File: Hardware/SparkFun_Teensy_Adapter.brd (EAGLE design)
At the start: 53.3 x 59.7 mm, 19 parts, among them U1 5V

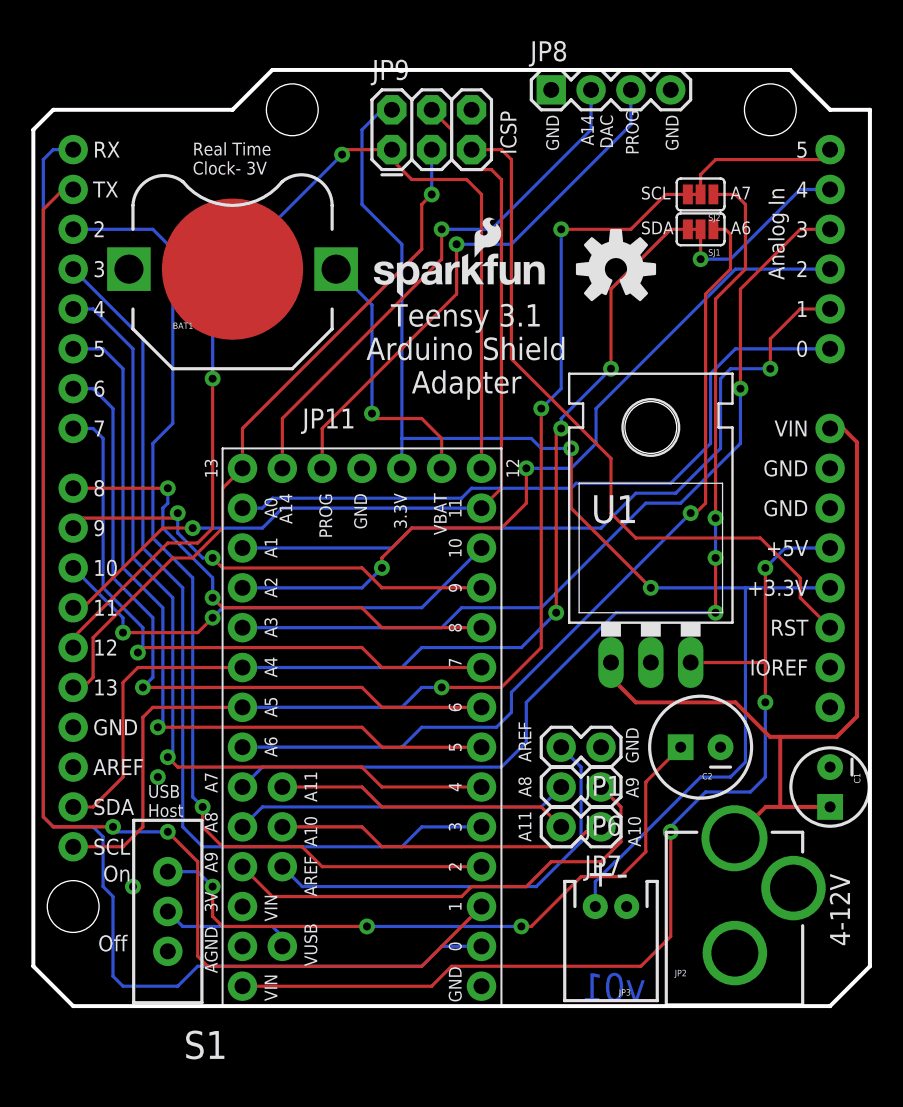
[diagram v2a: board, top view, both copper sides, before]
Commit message: Moving vias from under regulator, removing USB host shield parts
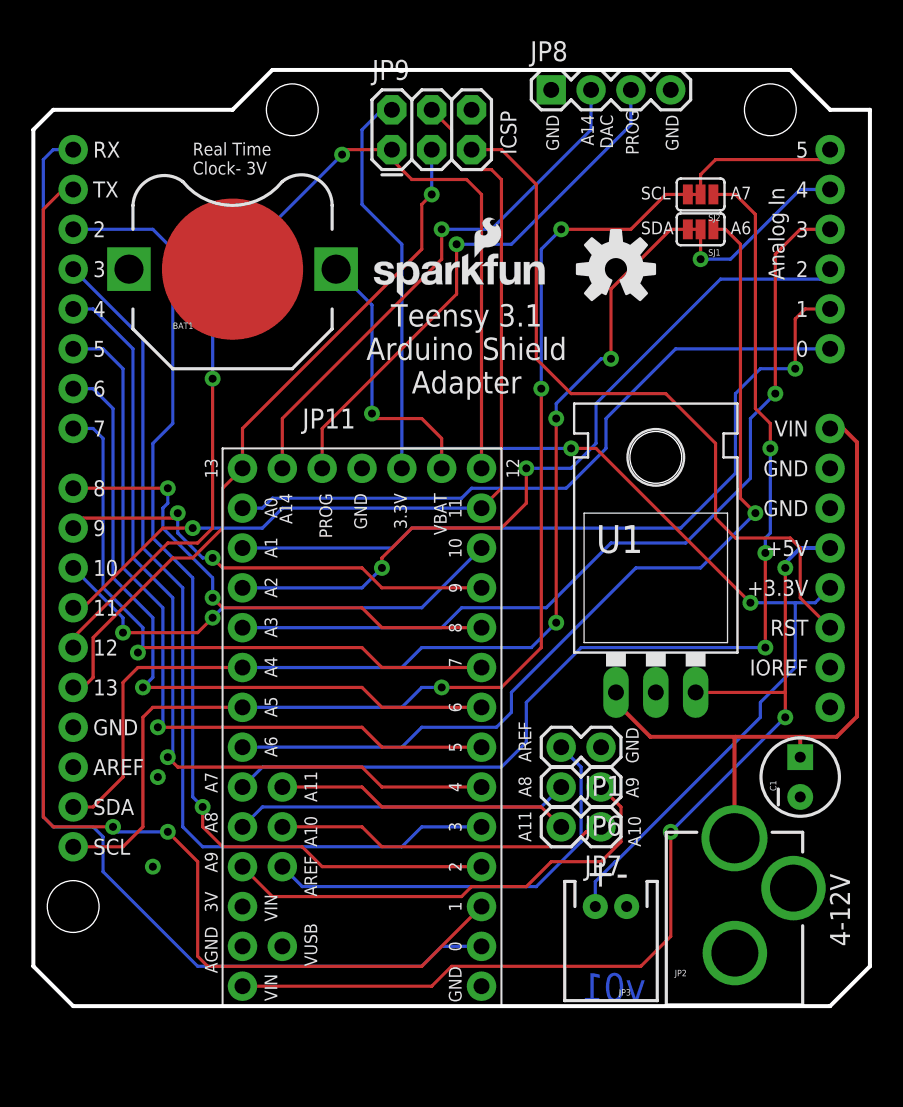
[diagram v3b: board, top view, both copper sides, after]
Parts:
- removed C2: 100uF, SparkFun-Capacitors:CPOL-RADIAL-100UF-25V
- removed S1: (no value), SparkFun-Electromechanical:SWITCH-SPDT
- JP1, JP6, JP7: value M02PTH -> (none)
- JP11: value TEENSY-3.1 -> TEENSY-3.1SILK
- JP3: value M02JST-PTH-2 -> (none)
- moved C1 2.01 mm to (51.4, 31.1), turned to 90 degrees
- moved U1 1.93 mm to (42.2, 40.3)
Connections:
- removed net N$1: C2.1, S1.3
- net GND: no longer C2.2
- net VUSB: no longer S1.2
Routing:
- net N$1: track 42.6 -> 0.00 mm, vias 3 -> 0
- net VUSB: track 8.60 -> 0.00 mm
- net VRAW: track 49.7 -> 44.8 mm
- net RX: track 82.4 -> 77.8 mm
- net A7: track 65.4 -> 69.9 mm
- net A6: track 55.7 -> 59.3 mm
- net 3.3V: track 84.0 -> 81.5 mm
- net A3: track 53.8 -> 55.4 mm
- net A0: track 44.3 -> 42.8 mm
- net 5V: track 65.7 -> 64.4 mm
- net A1: track 47.5 -> 48.6 mm
- net RESET: track 45.7 -> 46.6 mm
- net SDA: track 68.0 -> 68.8 mm
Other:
- board text removed: "Off"
- board text removed: "On"
- board text removed: "USB Host"

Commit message: Updates for QC final review before reds
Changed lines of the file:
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@@
 <setting verticaltext="up"/>
 </settings>
-<grid distance="0.0125" unitdist="inch" unit="inch" style="lines" multiple="1" display="yes" altdistance="0.005" altunitdist="inch" altunit="inch"/>
+<grid distance="0.05" unitdist="inch" unit="inch" style="lines" multiple="1" display="yes" altdistance="0.005" altunitdist="inch" altunit="inch"/>
 <layers>
 <layer number="1" name="Top" color="4" fill="1" visible="yes" active="yes"/>
@@
 <layer number="47" name="Measures" color="7" fill="1" visible="no" active="yes"/>
 <layer number="48" name="Document" color="7" fill="1" visible="no" active="yes"/>
-<layer number="49" name="Reference" color="7" fill="1" visible="no" active="yes"/>
+<layer number="49" name="Reference" color="7" fill="1" visible="yes" active="yes"/>
 <layer number="50" name="dxf" color="7" fill="1" visible="no" active="no"/>
 <layer number="51" name="tDocu" color="6" fill="1" visible="yes" active="yes"/>
@@
 <layer number="127" name="_tValues" color="7" fill="1" visible="no" active="yes"/>
 <layer number="128" name="_bValues" color="7" fill="1" visible="no" active="yes"/>
-<layer number="129" name="Mask" color="7" fill="1" visible="yes" active="yes"/>
+<layer number="129" name="Mask" color="7" fill="1" visible="no" active="yes"/>
 <layer number="131" name="tAdjust" color="7" fill="1" visible="no" active="yes"/>
 <layer number="132" name="bAdjust" color="7" fill="1" visible="no" active="yes"/>
@@
 Clock- 3V</text>
 <text x="33.3375" y="70.8025" size="1.016" layer="21" font="vector" ratio="15" rot="R90">ICSP</text>
-<wire x1="2.54" y1="19.05" x2="5.08" y2="16.51" width="0.254" layer="20"/>
-<wire x1="5.08" y1="16.51" x2="53.34" y2="16.51" width="0.254" layer="20"/>
-<wire x1="53.34" y1="16.51" x2="55.88" y2="19.05" width="0.254" layer="20"/>
-<wire x1="55.88" y1="19.05" x2="55.88" y2="73.66" width="0.254" layer="20"/>
-<wire x1="55.88" y1="73.66" x2="53.34" y2="73.66" width="0.254" layer="20"/>
-<wire x1="53.34" y1="73.66" x2="50.8" y2="76.2" width="0.254" layer="20"/>
-<wire x1="50.8" y1="76.2" x2="17.78" y2="76.2" width="0.254" layer="20"/>
-<wire x1="17.78" y1="76.2" x2="15.24" y2="73.66" width="0.254" layer="20"/>
-<wire x1="15.24" y1="73.66" x2="3.81" y2="73.66" width="0.254" layer="20"/>
-<wire x1="3.81" y1="73.66" x2="2.54" y2="72.39" width="0.254" layer="20"/>
-<wire x1="2.54" y1="72.39" x2="2.54" y2="19.05" width="0.254" layer="20"/>
+<wire x1="2.54" y1="19.05" x2="5.08" y2="16.51" width="0.2032" layer="20"/>
+<wire x1="5.08" y1="16.51" x2="53.34" y2="16.51" width="0.2032" layer="20"/>
+<wire x1="53.34" y1="16.51" x2="55.88" y2="19.05" width="0.2032" layer="20"/>
+<wire x1="55.88" y1="19.05" x2="55.88" y2="73.66" width="0.2032" layer="20"/>
+<wire x1="55.88" y1="73.66" x2="53.34" y2="73.66" width="0.2032" layer="20"/>
+<wire x1="53.34" y1="73.66" x2="50.8" y2="76.2" width="0.2032" layer="20"/>
+<wire x1="50.8" y1="76.2" x2="17.78" y2="76.2" width="0.2032" layer="20"/>
+<wire x1="17.78" y1="76.2" x2="15.24" y2="73.66" width="0.2032" layer="20"/>
+<wire x1="15.24" y1="73.66" x2="3.81" y2="73.66" width="0.2032" layer="20"/>
+<wire x1="3.81" y1="73.66" x2="2.54" y2="72.39" width="0.2032" layer="20"/>
+<wire x1="2.54" y1="72.39" x2="2.54" y2="19.05" width="0.2032" layer="20"/>
 <text x="34.29" y="32.0675" size="0.8128" layer="22" font="vector" ratio="15" rot="MR90" align="top-left">AREF</text>
 <text x="34.29" y="29.845" size="0.8128" layer="22" font="vector" ratio="15" rot="MR90" align="top-left">A8</text>
@@
 <elements>
 <element name="FRAME1" library="SparkFun-Aesthetics" package="CREATIVE_COMMONS" value="" x="3.81" y="-10.16">
-<attribute name="VERSION" value="v01" x="41.5925" y="16.8275" size="1.778" layer="16" font="vector" ratio="15" rot="MR0"/>
-<attribute name="DESIGNER" value="Toni Klopfenstein" x="30.48" y="-10.16" size="1.778" layer="51"/>
+<attribute name="VERSION" value="v10" x="41.5925" y="16.8275" size="1.778" layer="16" font="vector" ratio="15" rot="MR0"/>
+<attribute name="DESIGNER" value="Toni Klopfenstein" x="34.29" y="-10.16" size="1.778" layer="51"/>
 </element>
 <element name="JP10" library="Testing" package="UNO_R3_SHIELD_HOLES" value="ARDUINO_R3_SHIELDUNO_R3_SHIELD_HOLES" x="2.54" y="16.51"/>

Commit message: Value Changes for 3D Modeling
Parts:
- BAT1: value (none) -> CoinCell
- JP3: value (none) -> JST2
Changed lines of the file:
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@@
 <?xml version="1.0" encoding="utf-8"?>
 <!DOCTYPE eagle SYSTEM "eagle.dtd">
-<eagle version="7.2.0">
+<eagle version="7.7.0">
 <drawing>
 <settings>
@@
 <layer number="23" name="tOrigins" color="15" fill="1" visible="yes" active="yes"/>
 <layer number="24" name="bOrigins" color="15" fill="1" visible="yes" active="yes"/>
-<layer number="25" name="tNames" color="7" fill="1" visible="no" active="yes"/>
-<layer number="26" name="bNames" color="7" fill="1" visible="no" active="yes"/>
-<layer number="27" name="tValues" color="7" fill="1" visible="no" active="yes"/>
-<layer number="28" name="bValues" color="7" fill="1" visible="no" active="yes"/>
+<layer number="25" name="tNames" color="7" fill="1" visible="yes" active="yes"/>
+<layer number="26" name="bNames" color="7" fill="1" visible="yes" active="yes"/>
+<layer number="27" name="tValues" color="7" fill="1" visible="yes" active="yes"/>
+<layer number="28" name="bValues" color="7" fill="1" visible="yes" active="yes"/>
 <layer number="29" name="tStop" color="7" fill="3" visible="no" active="yes"/>
 <layer number="30" name="bStop" color="7" fill="6" visible="no" active="yes"/>
@@
 <attribute name="PROD_ID" value="CONN-08197" x="47.244" y="13.335" size="1.778" layer="27" font="vector" ratio="15" display="off"/>
 </element>
-<element name="JP3" library="SparkFun-Connectors" package="JST-2-PTH" value="" x="39.37" y="22.86" rot="R180">
+<element name="JP3" library="SparkFun-Connectors" package="JST-2-PTH" value="JST2" x="39.37" y="22.86" rot="R180">
 <attribute name="PROD_ID" value="CONN-09863" x="39.37" y="22.86" size="1.778" layer="27" font="vector" ratio="15" rot="R180" display="off"/>
 <attribute name="SKU" value="PRT-09914" x="39.37" y="22.86" size="1.778" layer="27" font="vector" ratio="15" rot="R180" display="off"/>
@@
 <element name="JP7" library="SparkFun-Connectors" package="1X02" value="" x="38.735" y="27.94" rot="R180"/>
 <element name="JP8" library="SparkFun-Connectors" package="1X04" value="" x="35.56" y="74.93"/>
-<element name="BAT1" library="SparkFun-Electromechanical" package="BATTCON_12MM_PTH" value="" x="15.24" y="63.5">
+<element name="BAT1" library="SparkFun-Electromechanical" package="BATTCON_12MM_PTH" value="CoinCell" x="15.24" y="63.5">
 <attribute name="PROD_ID" value="BATT-08315" x="15.24" y="63.5" size="1.778" layer="27" display="off"/>
 </element>

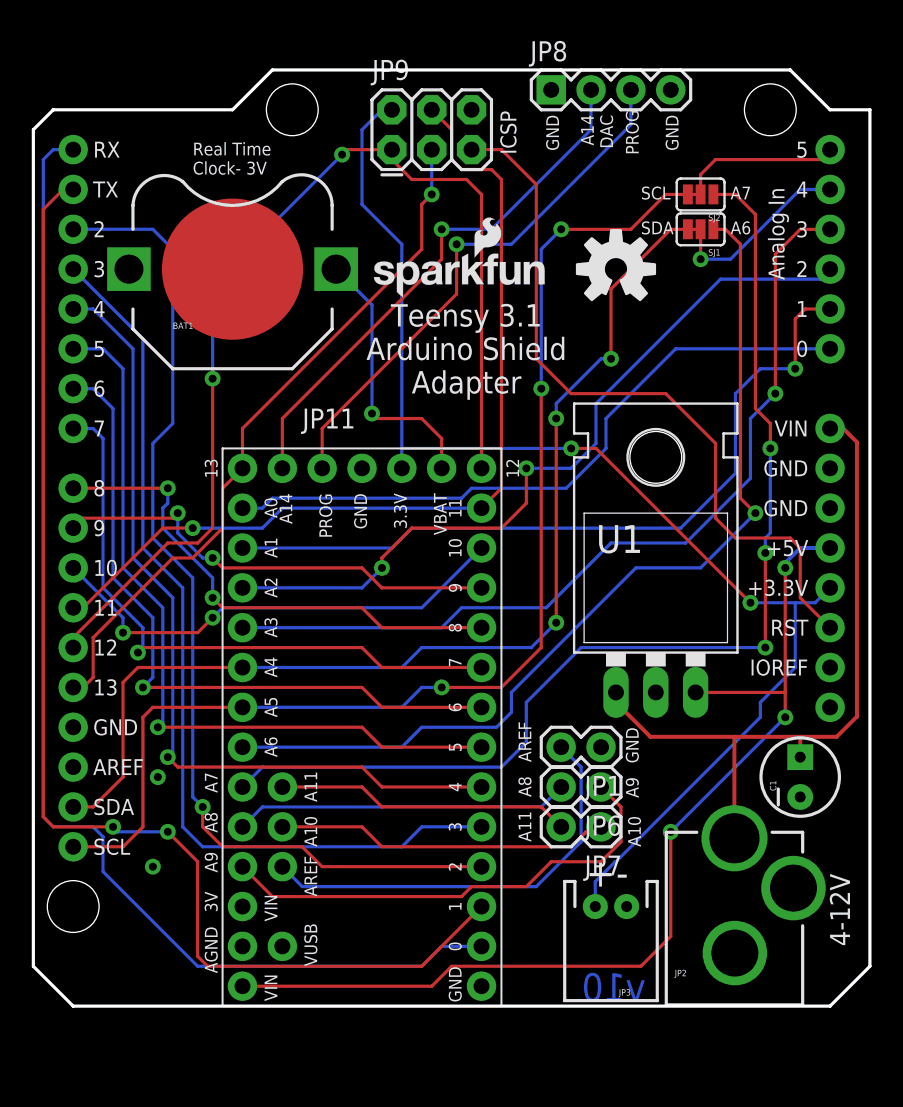
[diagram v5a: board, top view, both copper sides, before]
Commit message: Remove ISP connection to 3.3V. Add NO jumper connection.
Request by PaulS. When a shield was attached via SPI the 5V from the shield would kill the 3.3V Teensy.
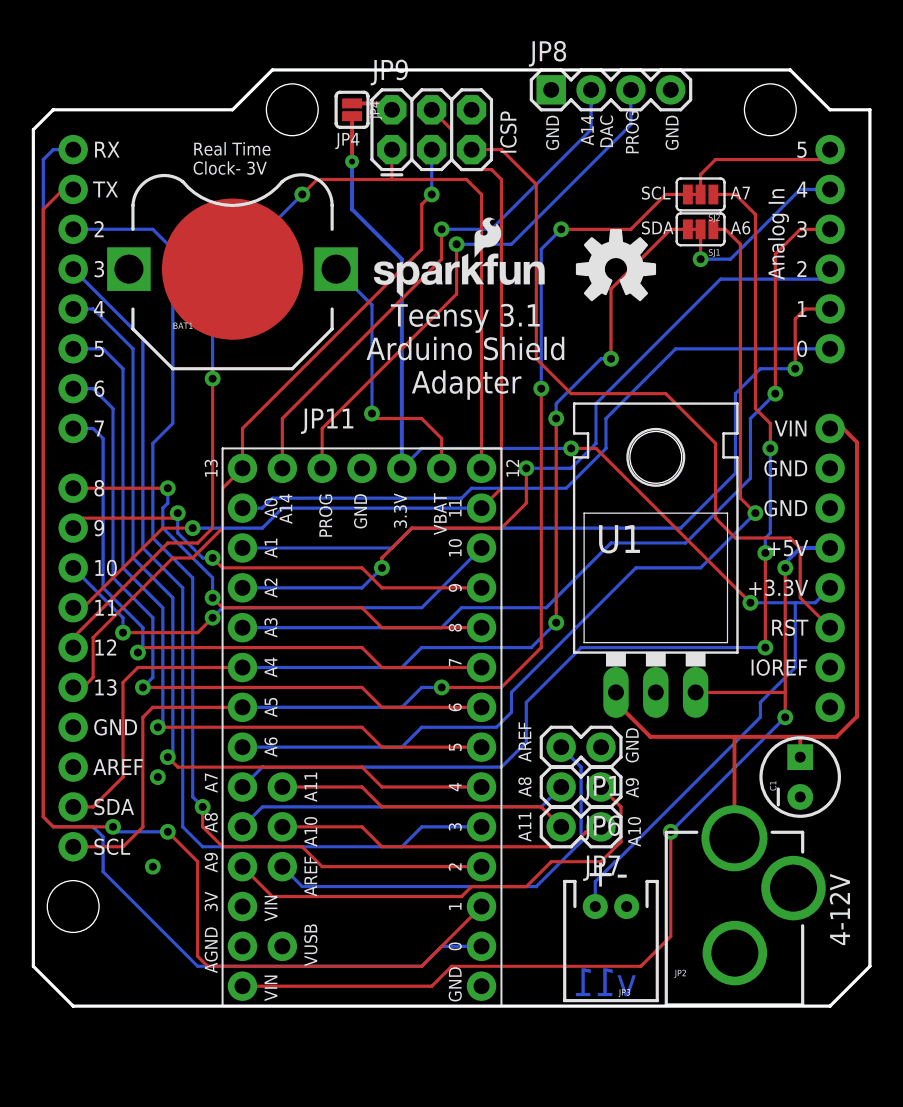
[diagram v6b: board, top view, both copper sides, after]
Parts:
- added JP4: (no value), SparkFun-Jumpers:SMT-JUMPER_2_NO_SILK
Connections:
- new net N$1: JP4.1, JP9.2
- net 3.3V: now also JP4.2; no longer JP9.2
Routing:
- net N$1: track 0.00 -> 2.71 mm
- net 3.3V: track 81.5 -> 80.7 mm, vias 2 -> 3
- net MISO: track 67.7 -> 68.3 mm
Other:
- board text added: "JP4"
- board text added: "v11"
